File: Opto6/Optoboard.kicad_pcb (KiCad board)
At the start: 2 copper layers, 86 x 33.1 mm, 54 parts, among them J1 S1 Connector, J2 S2 Connector, J3 S3 Connector, J4 S4 Connector, J6 S5 Connector, J7 S6 Connector, P1 CONN_01X08, P2 CONN_01X02, U1 6N135, U2 6N135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

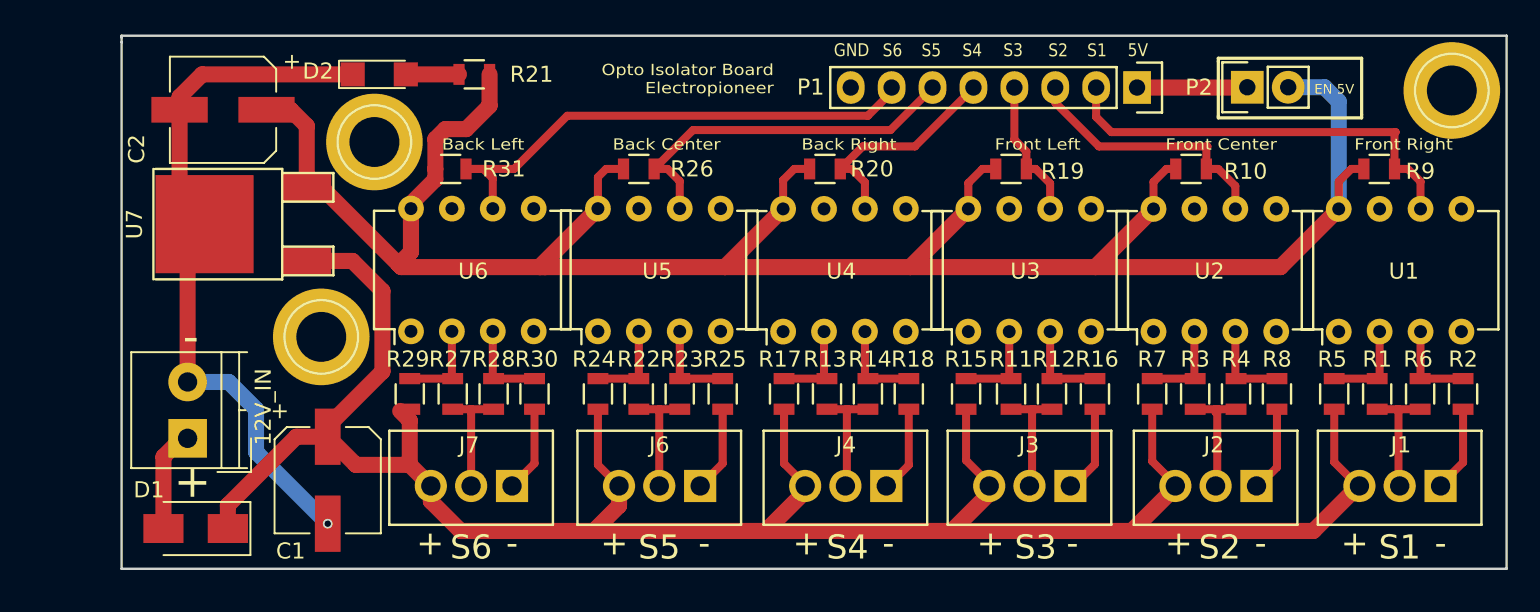
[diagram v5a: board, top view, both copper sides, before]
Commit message: Modified to 3.3V and 5V compatibility
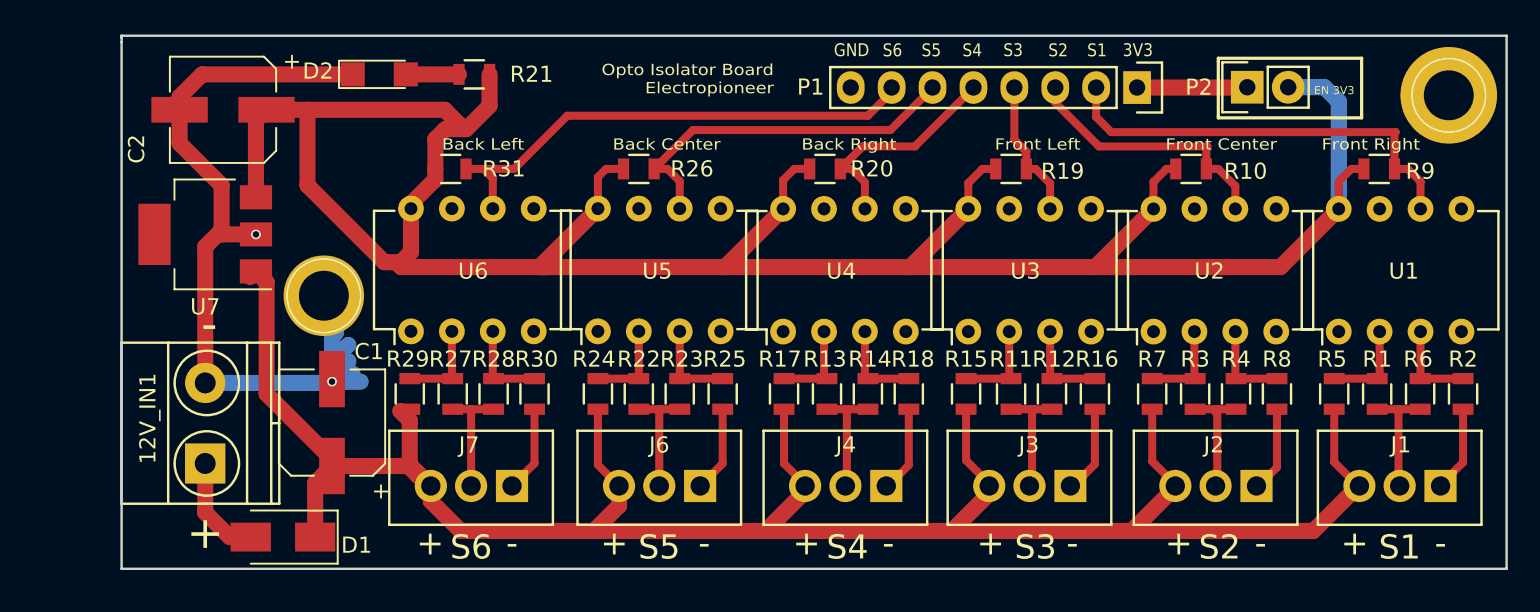
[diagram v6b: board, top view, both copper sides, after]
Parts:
- removed 12V_IN: Screw_Terminal_01x02, Connectors_Terminal_Blocks:TerminalBlock_4UCON_19963_02x3.5mm_Straight
- removed the REF** at (224.5, 93.5)
- removed the REF** at (154.3, 108.8)
- removed the REF** at (157.6, 96.7)
- added 12V_IN1: Screw_Terminal_01x02, Connectors_Terminal_Blocks:TerminalBlock_Pheonix_MKDS1.5-2pol, F.Cu at (147.1, 116.7)
- added REF**: 1pin, Connectors:1pin, F.Cu at (224.3, 93.8)
- added REF**: 1pin, Connectors:1pin, F.Cu at (154.5, 106.3)
- U7: value L7805 -> LM2937ET-3.3; footprint TO_SOT_Packages_SMD:TO-252-2Lead -> TO_SOT_Packages_SMD:SOT-223
- moved U7 6.34 mm to (147.1, 102.5), turned to 180 degrees
- moved D1 5.45 mm to (151.9, 121.3)
- moved C1 3.59 mm to (155.0, 114.1), turned to 90 degrees
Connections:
- net +5V renamed +3V3
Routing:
- net +3V3: track 175.5 -> 193.5 mm
- net GND: track 76.6 -> 84.3 mm, vias 1 -> 2
- net +12V: track 143.6 -> 136.6 mm
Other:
- board text added: "3V3"
- board text added: "EN 3V3"
- board text added: "Opto-isolator board Rev: 1.1 - Opto version: 6"
- board text removed: "5V"
- board text removed: "EN 5V"
- board text removed: "Opto-isolator board Rev: 1.0 - Opto version: 6"

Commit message: Added pdf and images
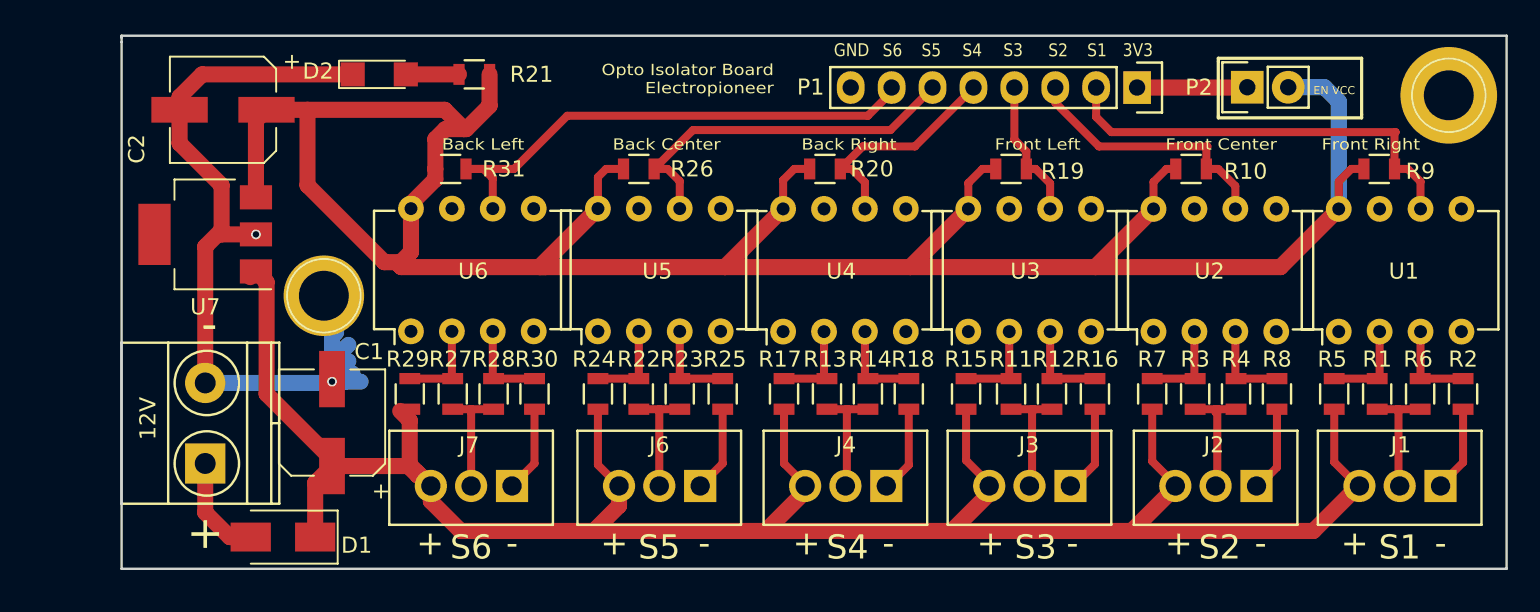
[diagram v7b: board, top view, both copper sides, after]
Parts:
- added G***: LOGO, Hardware:EP_Logo_3, B.Cu at (149.3, 97.3)
- 12V : renamed from 12V_IN1
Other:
- board text added: "EN VCC"
- board text removed: "EN 3V3"

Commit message: Updated the regulator and some small modifs
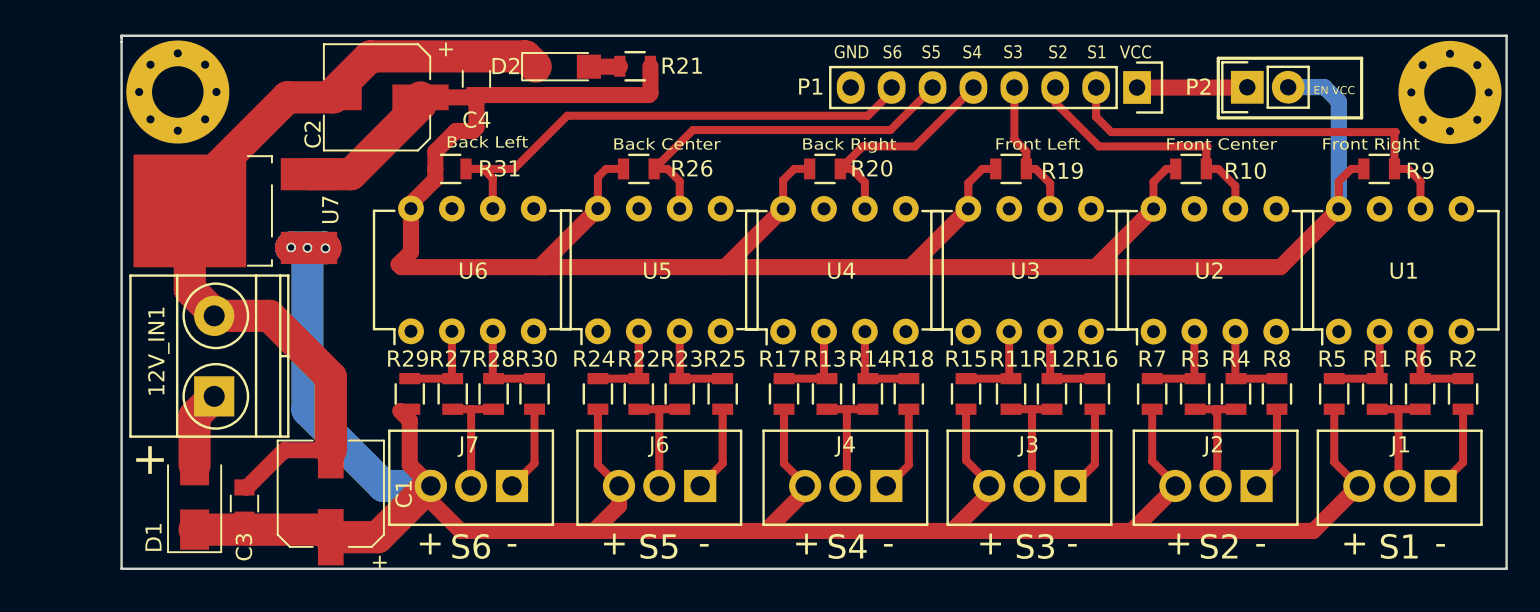
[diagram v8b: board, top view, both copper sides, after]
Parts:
- removed REF** (x2): 1pin, Connectors:1pin
- added C3: 100n, Capacitors_SMD:C_0805, F.Cu at (149.6, 119.2)
- added C4: 100n, Capacitors_SMD:C_0805, F.Cu at (164.0, 92.8)
- added MK1: Mounting_Hole, Mounting_Holes:MountingHole_3.2mm_M3_Pad_Via, F.Cu at (145.4, 93.6)
- added MK2: Mounting_Hole, Mounting_Holes:MountingHole_3.2mm_M3_Pad_Via, F.Cu at (224.4, 93.6)
- 12V_IN1: renamed from 12V 
- C1: value 470u -> 100u
- C2: value 470uF -> 100u
- U7: value LM2937ET-3.3 -> LM7805; footprint TO_SOT_Packages_SMD:SOT-223 -> TO_SOT_Packages_SMD:TO-252-2Lead
- moved D2 11.4 mm to (169.3, 92.0)
- moved R21 10.0 mm to (173.8, 92.0)
- moved C2 9.59 mm to (157.8, 94.0)
- moved D1 6.01 mm to (146.5, 118.8), turned to 90 degrees
- moved G*** 5.49 mm to (154.5, 95.6)
- moved C1 4.42 mm to (154.9, 118.6)
- moved 12V_IN1 4.20 mm to (147.7, 112.5)
- moved U7 3.10 mm to (149.9, 101.0)
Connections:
- net +3V3 renamed VCC
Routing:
- net +12V: track 136.6 -> 153.5 mm, vias 0 -> 3
- net VCC: track 193.5 -> 184.6 mm
- net Net-(12V_IN1-Pad1): track 6.51 -> 4.78 mm
- net Net-(D2-Pad2): track 3.30 -> 1.93 mm
- net GND: track 84.3 -> 85.6 mm, vias 2 -> 0
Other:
- board text added: "Opto-isolator board Rev: 1.2 - Opto version: 6"
- board text added: "VCC"
- board text removed: "3V3"
- board text removed: "Opto Isolator Board Electropioneer"
- board text removed: "Opto-isolator board Rev: 1.1 - Opto version: 6"
